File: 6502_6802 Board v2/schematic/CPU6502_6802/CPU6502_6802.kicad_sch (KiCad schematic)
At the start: 32 parts, among them J5 Conn_01x09, J6 Conn_01x08, J7 Conn_01x08, J8 Conn_01x09, J9 Conn_02x05_Odd_Even, U1 XC9572VQ44, U7 W65C02SxP, U99 MC6802

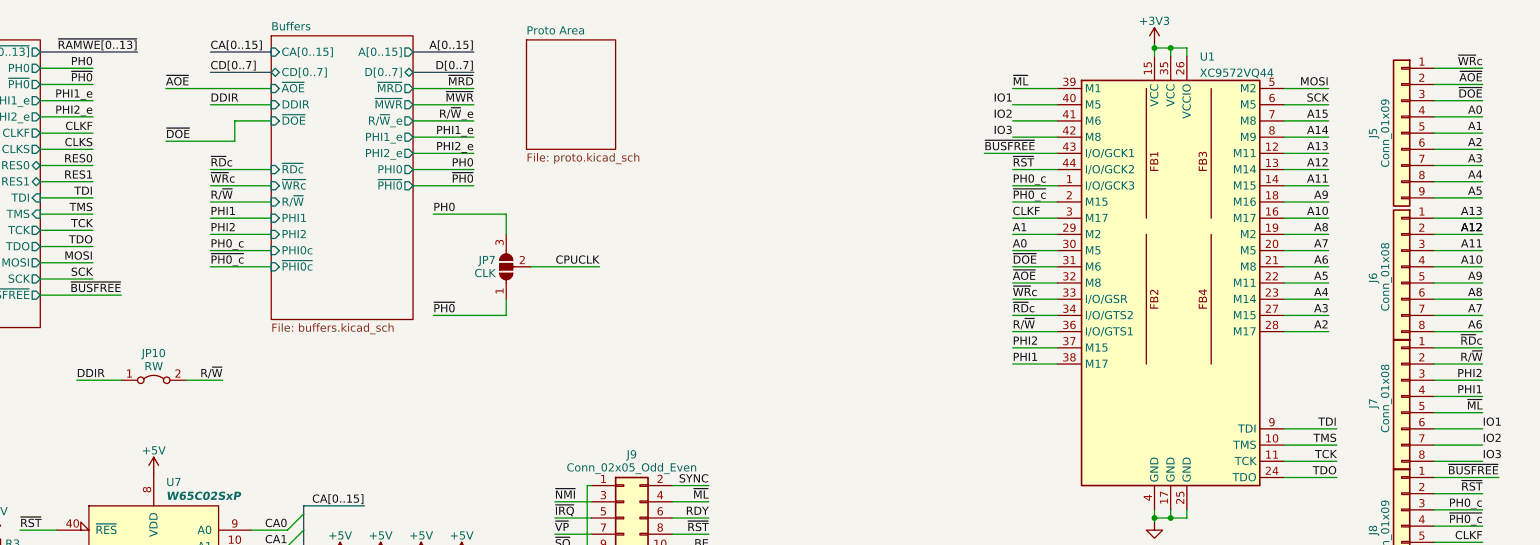
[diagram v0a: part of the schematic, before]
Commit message: Documentation update, 6800 working, new computers added
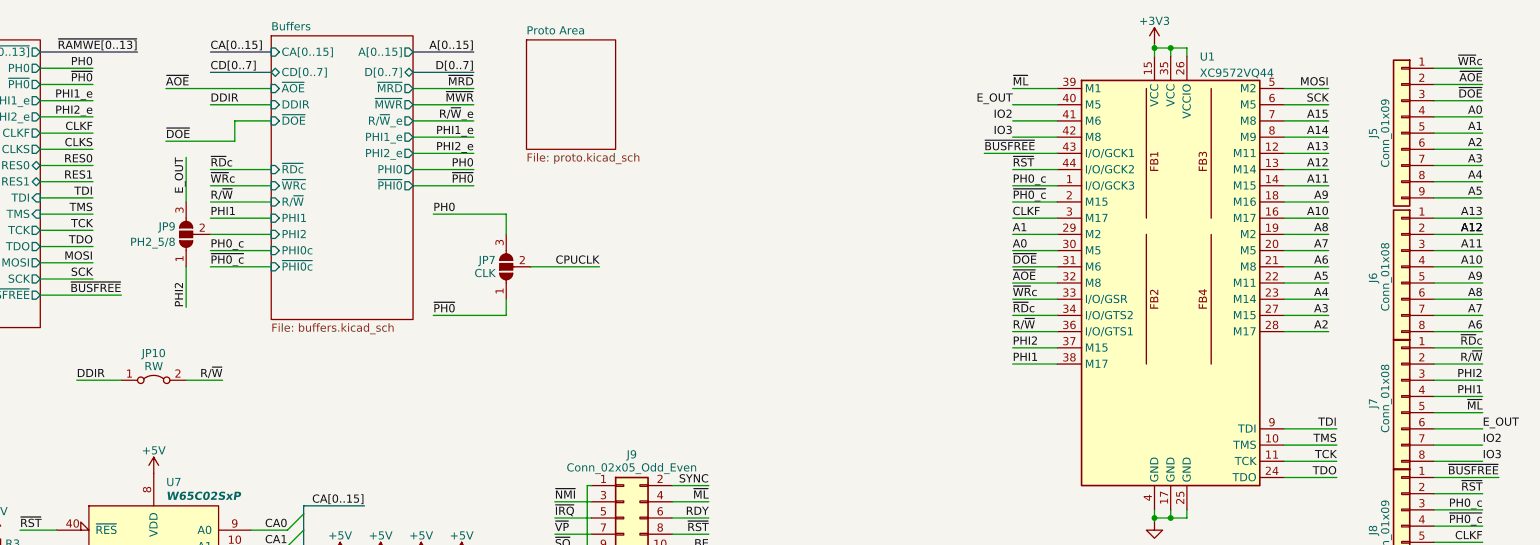
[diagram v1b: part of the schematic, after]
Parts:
- added JP9: PH2_5/8, Jumper:SolderJumper-3_P1.3mm_Open_RoundedPad1.0x1.5mm_NumberLabels, symbol Jumper:SolderJumper_3_Open
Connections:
- net PHI2: now also JP9.1 (A)
- net IO1 renamed E_OUT
- net E_OUT: now also JP9.3 (B)
- new net Buffers/PHI2: JP9.2 (C)
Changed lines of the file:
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@@
+    (stroke (width 0) (type default))
+  )
+  (wire (pts (xy 74.295 52.07) (xy 74.295 58.42))
     (stroke (width 0) (type default))
   )
@@
   )
   (wire (pts (xy 14.605 51.435) (xy 22.86 51.435))
+    (stroke (width 0) (type default))
+  )
+  (wire (pts (xy 74.295 34.925) (xy 74.295 41.91))
     (stroke (width 0) (type default))
   )
@@
     (effects (font (size 1.27 1.27)) (justify left bottom))
   )
-  (label "PHI2" (at 78.105 46.99 0) (fields_autoplaced)
+  (label "PHI2" (at 74.295 58.42 90) (fields_autoplaced)
     (effects (font (size 1.27 1.27)) (justify left bottom))
   )
@@
     (effects (font (size 1.27 1.27)) (justify right bottom))
   )
-  (label "IO1" (at 203.835 26.67 180) (fields_autoplaced)
+  (label "E_OUT" (at 203.835 26.67 180) (fields_autoplaced)
     (effects (font (size 1.27 1.27)) (justify right bottom))
   )
@@
     (effects (font (size 1.27 1.27)) (justify right bottom))
   )
-  (label "IO1" (at 277.495 77.47 0) (fields_autoplaced)
+  (label "E_OUT" (at 277.495 77.47 0) (fields_autoplaced)
     (effects (font (size 1.27 1.27)) (justify left bottom))
   )
@@
   (label "~{RST}" (at 48.26 93.345 0) (fields_autoplaced)
     (effects (font (size 1.27 1.27)) (justify left bottom))
+  )
+  (label "E_OUT" (at 74.295 34.925 270) (fields_autoplaced)
+    (effects (font (size 1.27 1.27)) (justify right bottom))
   )
   (label "R{slash}~{W}" (at 80.01 69.85 180) (fields_autoplaced)
@@
         )
       )
+    )
+  )
+  (symbol (lib_id "Jumper:SolderJumper_3_Open") (at 74.295 46.99 90) (unit 1)
+    (in_bom yes) (on_board yes) (dnp no) (fields_autoplaced)
+    (property "Reference" "JP9" (at 72.6441 45.7779 90)
+      (effects (font (size 1.27 1.27)) (justify left))
+    )
+    (property "Value" "PH2_5/8" (at 72.6441 48.2021 90)
+      (effects (font (size 1.27 1.27)) (justify left))
+    )
+    (property "Footprint" "Jumper:SolderJumper-3_P1.3mm_Open_RoundedPad1.0x1.5mm_NumberLabels" (at 74.295 46.99 0)
+      (effects (font (size 1.27 1.27)) hide)
+    )
+    (property "Datasheet" "~" (at 74.295 46.99 0)
+      (effects (font (size 1.27 1.27)) hide)
+    )
+    (pin "1")
+    (pin "2")
+    (pin "3")
+    (instances
+      (project "CPU6502_6802"
+        (path "/2eaa3998-c9cb-43b1-9b23-df656c8158b0"
+          (reference "JP9") (unit 1)
+        )
+      )

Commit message: DREAM6800 video started
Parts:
- added R12: 10k, Resistor_SMD:R_1206_3216Metric_Pad1.30x1.75mm_HandSolder, symbol Device:R_Small
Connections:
- net IO2 is gone; now on net RDY: J7.7 (Pin_7), U1.41 (M6)
- net IO3 is gone; now on net SYNC: J7.8 (Pin_8), U1.42 (M8)
- net +3V3: now also R12.1
- net A0 renamed HALT_in
- net HALT_in: now also R12.2
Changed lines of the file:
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@@
     (title "Unicomp v2 - 6502 6802 Board")
     (date "2023-07-06")
-    (rev "v1")
+    (rev "v1.1")
     (company "100% Offner")
     (comment 1 "v1: Initial")
+    (comment 2 "v1.1: added f. 6802: HALT, BA, VMA")
   )
   (junction (at 232.41 160.02) (diameter 0) (color 0 0 0 0)
@@
   (junction (at 29.21 94.615) (diameter 0) (color 0 0 0 0)
   )
+  (junction (at 198.12 49.53) (diameter 0) (color 0 0 0 0)
+  )
   (junction (at 241.3 160.02) (diameter 0) (color 0 0 0 0)
   )
@@
     (stroke (width 0) (type default))
   )
+  (wire (pts (xy 198.12 49.53) (xy 210.82 49.53))
+    (stroke (width 0) (type default))
+  )
   (wire (pts (xy 84.455 149.225) (xy 90.17 149.225))
     (stroke (width 0) (type default))
@@
     (stroke (width 0) (type default))
   )
+  (wire (pts (xy 198.12 48.895) (xy 198.12 49.53))
+    (stroke (width 0) (type default))
+  )
   (wire (pts (xy 228.6 91.44) (xy 231.14 91.44))
     (stroke (width 0) (type default))
@@
     (stroke (width 0) (type default))
   )
-  (wire (pts (xy 203.835 49.53) (xy 210.82 49.53))
+  (wire (pts (xy 189.865 49.53) (xy 198.12 49.53))
     (stroke (width 0) (type default))
   )
@@
     (effects (font (size 1.27 1.27)) (justify right bottom))
   )
+  (label "SYNC" (at 277.495 82.55 180) (fields_autoplaced)
+    (effects (font (size 1.27 1.27)) (justify right bottom))
+  )
   (label "A11" (at 253.365 39.37 180) (fields_autoplaced)
     (effects (font (size 1.27 1.27)) (justify right bottom))
@@
     (effects (font (size 1.27 1.27)) (justify right bottom))
   )
+  (label "RDY" (at 203.835 29.21 0) (fields_autoplaced)
+    (effects (font (size 1.27 1.27)) (justify left bottom))
+  )
   (label "PH0_c" (at 277.495 90.17 180) (fields_autoplaced)
     (effects (font (size 1.27 1.27)) (justify right bottom))
@@
     (effects (font (size 1.27 1.27)) (justify left bottom))
   )
+  (label "HALT_in" (at 277.495 28.575 180) (fields_autoplaced)
+    (effects (font (size 1.27 1.27)) (justify right bottom))
+  )
   (label "CLKS" (at 59.69 33.655 180) (fields_autoplaced)
     (effects (font (size 1.27 1.27)) (justify right bottom))
@@
     (effects (font (size 1.27 1.27)) (justify right bottom))
   )
-  (label "A0" (at 203.835 49.53 0) (fields_autoplaced)
-    (effects (font (size 1.27 1.27)) (justify left bottom))
-  )
   (label "CD0" (at 90.17 136.525 180) (fields_autoplaced)
     (effects (font (size 1.27 1.27)) (justify right bottom))
@@
     (effects (font (size 1.27 1.27)) (justify right bottom))
   )
-  (label "E_OUT" (at 203.835 26.67 180) (fields_autoplaced)
-    (effects (font (size 1.27 1.27)) (justify right bottom))
+  (label "E_OUT" (at 203.835 26.67 0) (fields_autoplaced)
+    (effects (font (size 1.27 1.27)) (justify left bottom))
   )
   (label "~{RAMWE[0..13]}" (at 66.675 18.415 180) (fields_autoplaced)
@@
     (effects (font (size 1.27 1.27)) (justify left bottom))
   )
+  (label "SYNC" (at 203.835 31.75 0) (fields_autoplaced)
+    (effects (font (size 1.27 1.27)) (justify left bottom))
+  )
   (label "CD3" (at 130.81 130.81 0) (fields_autoplaced)
     (effects (font (size 1.27 1.27)) (justify left bottom))
@@
     (effects (font (size 1.27 1.27)) (justify right bottom))
   )
-  (label "IO3" (at 277.495 82.55 0) (fields_autoplaced)
-    (effects (font (size 1.27 1.27)) (justify left bottom))
-  )
   (label "CD2" (at 130.81 128.27 0) (fields_autoplaced)
     (effects (font (size 1.27 1.27)) (justify left bottom))
@@
     (effects (font (size 1.27 1.27)) (justify left bottom))
   )
+  (label "HALT_in" (at 189.865 49.53 0) (fields_autoplaced)
+    (effects (font (size 1.27 1.27)) (justify left bottom))
+  )
   (label "TDO" (at 59.69 48.895 180) (fields_autoplaced)
     (effects (font (size 1.27 1.27)) (justify right bottom))
@@
     (effects (font (size 1.27 1.27)) (justify right bottom))
   )
-  (label "E_OUT" (at 277.495 77.47 0) (fields_autoplaced)
-    (effects (font (size 1.27 1.27)) (justify left bottom))
+  (label "E_OUT" (at 277.495 77.47 180) (fields_autoplaced)
+    (effects (font (size 1.27 1.27)) (justify right bottom))
   )
   (label "CA15" (at 90.17 131.445 180) (fields_autoplaced)
@@
     (effects (font (size 1.27 1.27)) (justify left bottom))
   )
-  (label "IO3" (at 203.835 31.75 180) (fields_autoplaced)
-    (effects (font (size 1.27 1.27)) (justify right bottom))
-  )
   (label "CA6" (at 90.17 108.585 180) (fields_autoplaced)
     (effects (font (size 1.27 1.27)) (justify right bottom))
@@
     (effects (font (size 1.27 1.27)) (justify right bottom))
   )
-  (label "A0" (at 277.495 28.575 180) (fields_autoplaced)
-    (effects (font (size 1.27 1.27)) (justify right bottom))
-  )
   (label "~{RST}" (at 277.495 87.63 180) (fields_autoplaced)
     (effects (font (size 1.27 1.27)) (justify right bottom))
@@
     (effects (font (size 1.27 1.27)) (justify left bottom))
   )
-  (label "IO2" (at 203.835 29.21 180) (fields_autoplaced)
-    (effects (font (size 1.27 1.27)) (justify right bottom))
-  )
   (label "~{RST}" (at 48.26 93.345 0) (fields_autoplaced)
     (effects (font (size 1.27 1.27)) (justify left bottom))
@@
     (effects (font (size 1.27 1.27)) (justify left bottom))
   )
+  (label "RDY" (at 277.495 80.01 180) (fields_autoplaced)
+    (effects (font (size 1.27 1.27)) (justify right bottom))
+  )
   (label "CD[0..7]" (at 102.235 133.35 180) (fields_autoplaced)
     (effects (font (size 1.27 1.27)) (justify right bottom))
@@
     (effects (font (size 1.27 1.27)) (justify left bottom))
   )
-  (label "IO2" (at 277.495 80.01 0) (fields_autoplaced)
-    (effects (font (size 1.27 1.27)) (justify left bottom))
-  )
   (label "CA9" (at 90.17 116.205 180) (fields_autoplaced)
     (effects (font (size 1.27 1.27)) (justify right bottom))
@@
     )
   )
+  (symbol (lib_id "Device:R_Small") (at 198.12 46.355 0) (unit 1)
+    (in_bom yes) (on_board yes) (dnp no) (fields_autoplaced)
+    (property "Reference" "R12" (at 199.6186 45.5203 0)
+      (effects (font (size 1.27 1.27)) (justify left))
+    )
+    (property "Value" "10k" (at 199.6186 48.0572 0)
+      (effects (font (size 1.27 1.27)) (justify left))
+    )
+    (property "Footprint" "Resistor_SMD:R_1206_3216Metric_Pad1.30x1.75mm_HandSolder" (at 198.12 46.355 0)
+      (effects (font (size 1.27 1.27)) hide)
+    )
+    (property "Datasheet" "~" (at 198.12 46.355 0)
+      (effects (font (size 1.27 1.27)) hide)
+    )
+    (pin "1")
+    (pin "2")
+    (instances
+      (project "CPU6502_6802"
+        (path "/2eaa3998-c9cb-43b1-9b23-df656c8158b0"
+          (reference "R12") (unit 1)
+        )
+      )
+    )
+  )
   (symbol (lib_id "Device:C_Small") (at 276.225 156.845 0) (unit 1)
     (in_bom yes) (on_board yes) (dnp no) (fields_autoplaced)
@@
         )
       )
+    )
+  )
+  (symbol (lib_id "power:+3V3") (at 198.12 43.815 0) (unit 1)
+    (in_bom yes) (on_board yes) (dnp no) (fields_autoplaced)
+    (property "Reference" "#PWR018" (at 198.12 47.625 0)
+      (effects (font (size 1.27 1.27)) hide)
+    )
+    (property "Value" "+3V3" (at 198.12 40.2392 0)
+      (effects (font (size 1.27 1.27)))
+    )
+    (property "Footprint" "" (at 198.12 43.815 0)
+      (effects (font (size 1.27 1.27)) hide)
+    )
+    (property "Datasheet" "" (at 198.12 43.815 0)
+      (effects (font (size 1.27 1.27)) hide)
+    )
+    (pin "1")
+    (instances
+      (project "CPU6502_6802"
+        (path "/2eaa3998-c9cb-43b1-9b23-df656c8158b0"
+          (reference "#PWR018") (unit 1)
+        )
+      )

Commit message: Z80 added
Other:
- note added: "*"
- note added: "->"
- note added: "<-"
- note added: "~{RDc} <= NOT(R/~{W} AND PHI2) ~{WRc} <= NOT((NOT R/~{W}) AND PHI2) BUSFREE <= ~{RST} AND (PH0 OR PHI2) ~{AOE} <= NOT(~{BUSFREE}) ~{DOE} <= NOT(~{BUSFREE}) PH0 <= CLKF / 8 ~{PH0} <= NOT (PH0)"
- moved on the sheet: R12
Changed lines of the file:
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@@
   (junction (at 29.21 94.615) (diameter 0) (color 0 0 0 0)
   )
-  (junction (at 198.12 49.53) (diameter 0) (color 0 0 0 0)
+  (junction (at 188.595 49.53) (diameter 0) (color 0 0 0 0)
   )
   (junction (at 241.3 160.02) (diameter 0) (color 0 0 0 0)
@@
     (stroke (width 0) (type default))
   )
+  (wire (pts (xy 188.595 49.53) (xy 210.82 49.53))
+    (stroke (width 0) (type default))
+  )
   (wire (pts (xy 51.435 36.195) (xy 59.69 36.195))
     (stroke (width 0) (type default))
@@
     (stroke (width 0) (type default))
   )
-  (wire (pts (xy 198.12 49.53) (xy 210.82 49.53))
-    (stroke (width 0) (type default))
-  )
   (wire (pts (xy 84.455 149.225) (xy 90.17 149.225))
     (stroke (width 0) (type default))
@@
     (stroke (width 0) (type default))
   )
-  (wire (pts (xy 198.12 48.895) (xy 198.12 49.53))
+  (wire (pts (xy 188.595 48.895) (xy 188.595 49.53))
     (stroke (width 0) (type default))
   )
@@
     (stroke (width 0) (type default))
   )
-  (wire (pts (xy 189.865 49.53) (xy 198.12 49.53))
+  (wire (pts (xy 180.34 49.53) (xy 188.595 49.53))
     (stroke (width 0) (type default))
   )
@@
     (stroke (width 0) (type default))
   )
-  (image (at 172.085 29.21)
+  (image (at 166.37 24.765) (scale 0.865665)
     (data
       iVBORw0KGgoAAAANSUhEUgAAAfkAAAE/CAIAAADKZS0aAAAAA3NCSVQICAjb4U/gAAAgAElEQVR4
@@
     )
   )
+  (text "<-" (at 197.485 52.07 0)
+    (effects (font (size 1.27 1.27)) (justify left bottom))
+  )
+  (text "<-" (at 255.27 41.91 0)
+    (effects (font (size 1.27 1.27)) (justify left bottom))
+  )
+  (text "<-" (at 197.485 57.15 0)
+    (effects (font (size 1.27 1.27)) (justify left bottom))
+  )
   (text "JP1 closed: 6802 Ram disable\nJP2 6802: VCC STBY\nJP3 closed: 6802\nJP4, 5: 1-2: 6502, 2-3: 6802\nJP6: open for WD65C02 only!\n"
     (at 43.815 187.325 0)
     (effects (font (size 1.27 1.27)) (justify left bottom))
   )
+  (text "->" (at 197.485 46.99 0)
+    (effects (font (size 1.27 1.27)) (justify left bottom))
+  )
+  (text "<-" (at 255.27 24.13 0)
+    (effects (font (size 1.27 1.27)) (justify left bottom))
+  )
+  (text "~{RDc} <= NOT(R/~{W} AND PHI2)\n~{WRc} <= NOT((NOT R/~{W}) AND PHI2)\nBUSFREE <= ~{RST} AND (PH0 OR PHI2)\n~{AOE} <= NOT(~{BUSFREE})\n~{DOE} <= NOT(~{BUSFREE})\nPH0 <= CLKF / 8\n~{PH0} <= NOT (PH0) "
+    (at 210.82 123.825 0)
+    (effects (font (size 1.27 1.27)) (justify left bottom))
+  )
+  (text "<-" (at 197.485 59.69 0)
+    (effects (font (size 1.27 1.27)) (justify left bottom))
+  )
+  (text "<-" (at 197.485 41.91 0)
+    (effects (font (size 1.27 1.27)) (justify left bottom))
+  )
   (text "6802:\nRE: Ram Enable\nMR: Memory Read\nBA: Bus Available\nVMA: Valid Memory Address"
     (at 177.8 163.195 0)
     (effects (font (size 1.27 1.27)) (justify left bottom))
   )
+  (text "->" (at 197.485 44.45 0)
+    (effects (font (size 1.27 1.27)) (justify left bottom))
+  )
+  (text "<-" (at 255.27 36.83 0)
+    (effects (font (size 1.27 1.27)) (justify left bottom))
+  )
+  (text "->" (at 197.485 62.23 0)
+    (effects (font (size 1.27 1.27)) (justify left bottom))
+  )
+  (text "<-" (at 255.27 39.37 0)
+    (effects (font (size 1.27 1.27)) (justify left bottom))
+  )
+  (text "->" (at 198.12 36.83 0)
+    (effects (font (size 1.27 1.27)) (justify left bottom))
+  )
+  (text "<-" (at 255.27 26.67 0)
+    (effects (font (size 1.27 1.27)) (justify left bottom))
+  )
+  (text "<-" (at 255.27 62.23 0)
+    (effects (font (size 1.27 1.27)) (justify left bottom))
+  )
+  (text "<-" (at 255.27 49.53 0)
+    (effects (font (size 1.27 1.27)) (justify left bottom))
+  )
+  (text "<-" (at 255.27 46.99 0)
+    (effects (font (size 1.27 1.27)) (justify left bottom))
+  )
+  (text "*" (at 198.12 29.21 0)
+    (effects (font (size 1.27 1.27)) (justify left bottom))
+  )
+  (text "<-" (at 255.27 44.45 0)
+    (effects (font (size 1.27 1.27)) (justify left bottom))
+  )
+  (text "<-" (at 255.27 52.07 0)
+    (effects (font (size 1.27 1.27)) (justify left bottom))
+  )
+  (text "*" (at 175.895 49.53 0)
+    (effects (font (size 1.27 1.27)) (justify left bottom))
+  )
+  (text "->" (at 197.485 64.77 0)
+    (effects (font (size 1.27 1.27)) (justify left bottom))
+  )
+  (text "->" (at 198.12 24.13 0)
+    (effects (font (size 1.27 1.27)) (justify left bottom))
+  )
+  (text "<-" (at 255.27 34.29 0)
+    (effects (font (size 1.27 1.27)) (justify left bottom))
+  )
+  (text "<-" (at 255.27 54.61 0)
+    (effects (font (size 1.27 1.27)) (justify left bottom))
+  )
+  (text "<-" (at 255.27 59.69 0)
+    (effects (font (size 1.27 1.27)) (justify left bottom))
+  )
+  (text "<-" (at 197.485 39.37 0)
+    (effects (font (size 1.27 1.27)) (justify left bottom))
+  )
   (text "Job of CPLD:\nMake signals:\n~{MRD}, ~{MWR}, ~{AOE}, ~{DOE},\nPHI0 and ~{PHI0}.\nmake ~{HLT} Signal for Atari,\nRelease BUS when Reset,\nmake Signal ~{BUSFREE}."
-    (at 204.47 111.76 0)
+    (at 191.77 103.505 0)
+    (effects (font (size 1.27 1.27)) (justify left bottom))
+  )
+  (text "<-" (at 255.27 57.15 0)
+    (effects (font (size 1.27 1.27)) (justify left bottom))
+  )
+  (text "*" (at 198.12 31.75 0)
+    (effects (font (size 1.27 1.27)) (justify left bottom))
+  )
+  (text "->" (at 197.485 67.31 0)
+    (effects (font (size 1.27 1.27)) (justify left bottom))
+  )
+  (text "<-" (at 255.27 31.75 0)
+    (effects (font (size 1.27 1.27)) (justify left bottom))
+  )
+  (text "<-" (at 194.945 34.29 0)
+    (effects (font (size 1.27 1.27)) (justify left bottom))
+  )
+  (text "<-" (at 255.27 29.21 0)
     (effects (font (size 1.27 1.27)) (justify left bottom))
   )
@@
     (effects (font (size 1.27 1.27)) (justify left bottom))
   )
+  (text "<-" (at 197.485 54.61 0)
+    (effects (font (size 1.27 1.27)) (justify left bottom))
+  )
+  (text "<-" (at 197.485 26.67 0)
+    (effects (font (size 1.27 1.27)) (justify left bottom))
+  )
   (label "~{IOWR}" (at 14.605 31.115 0) (fields_autoplaced)
     (effects (font (size 1.27 1.27)) (justify left bottom))
@@
     (effects (font (size 1.27 1.27)) (justify left bottom))
   )
-  (label "HALT_in" (at 189.865 49.53 0) (fields_autoplaced)
+  (label "HALT_in" (at 180.34 49.53 0) (fields_autoplaced)
     (effects (font (size 1.27 1.27)) (justify left bottom))
   )
@@
     )
   )
-  (symbol (lib_id "Device:R_Small") (at 198.12 46.355 0) (unit 1)
+  (symbol (lib_id "Device:R_Small") (at 188.595 46.355 0) (unit 1)
     (in_bom yes) (on_board yes) (dnp no) (fields_autoplaced)
-    (property "Reference" "R12" (at 199.6186 45.5203 0)
+    (property "Reference" "R12" (at 190.0936 45.5203 0)
       (effects (font (size 1.27 1.27)) (justify left))
     )
-    (property "Value" "10k" (at 199.6186 48.0572 0)
+    (property "Value" "10k" (at 190.0936 48.0572 0)
       (effects (font (size 1.27 1.27)) (justify left))
     )
-    (property "Footprint" "Resistor_SMD:R_1206_3216Metric_Pad1.30x1.75mm_HandSolder" (at 198.12 46.355 0)
+    (property "Footprint" "Resistor_SMD:R_1206_3216Metric_Pad1.30x1.75mm_HandSolder" (at 188.595 46.355 0)
       (effects (font (size 1.27 1.27)) hide)
     )
-    (property "Datasheet" "~" (at 198.12 46.355 0)
+    (property "Datasheet" "~" (at 188.595 46.355 0)
       (effects (font (size 1.27 1.27)) hide)
     )
@@
     )
   )
-  (symbol (lib_id "power:+3V3") (at 198.12 43.815 0) (unit 1)
+  (symbol (lib_id "power:+3V3") (at 188.595 43.815 0) (unit 1)
     (in_bom yes) (on_board yes) (dnp no) (fields_autoplaced)
-    (property "Reference" "#PWR018" (at 198.12 47.625 0)
+    (property "Reference" "#PWR018" (at 188.595 47.625 0)
       (effects (font (size 1.27 1.27)) hide)
     )
-    (property "Value" "+3V3" (at 198.12 40.2392 0)
+    (property "Value" "+3V3" (at 188.595 40.2392 0)
       (effects (font (size 1.27 1.27)))
     )
-    (property "Footprint" "" (at 198.12 43.815 0)
+    (property "Footprint" "" (at 188.595 43.815 0)
       (effects (font (size 1.27 1.27)) hide)
     )
-    (property "Datasheet" "" (at 198.12 43.815 0)
+    (property "Datasheet" "" (at 188.595 43.815 0)
       (effects (font (size 1.27 1.27)) hide)
     )
